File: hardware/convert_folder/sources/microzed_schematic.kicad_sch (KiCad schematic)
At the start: 5 parts, among them J4 87832-1420

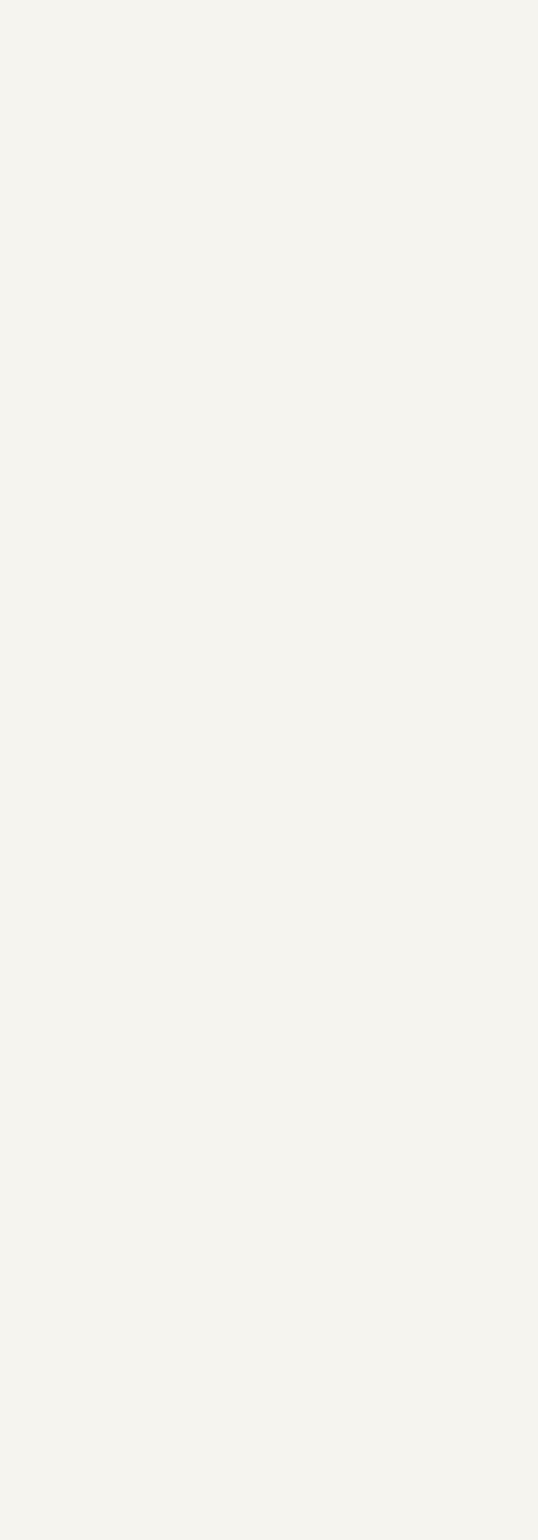
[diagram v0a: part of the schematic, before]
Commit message: fix: fix a lot of connections between blocks. Many more to go...
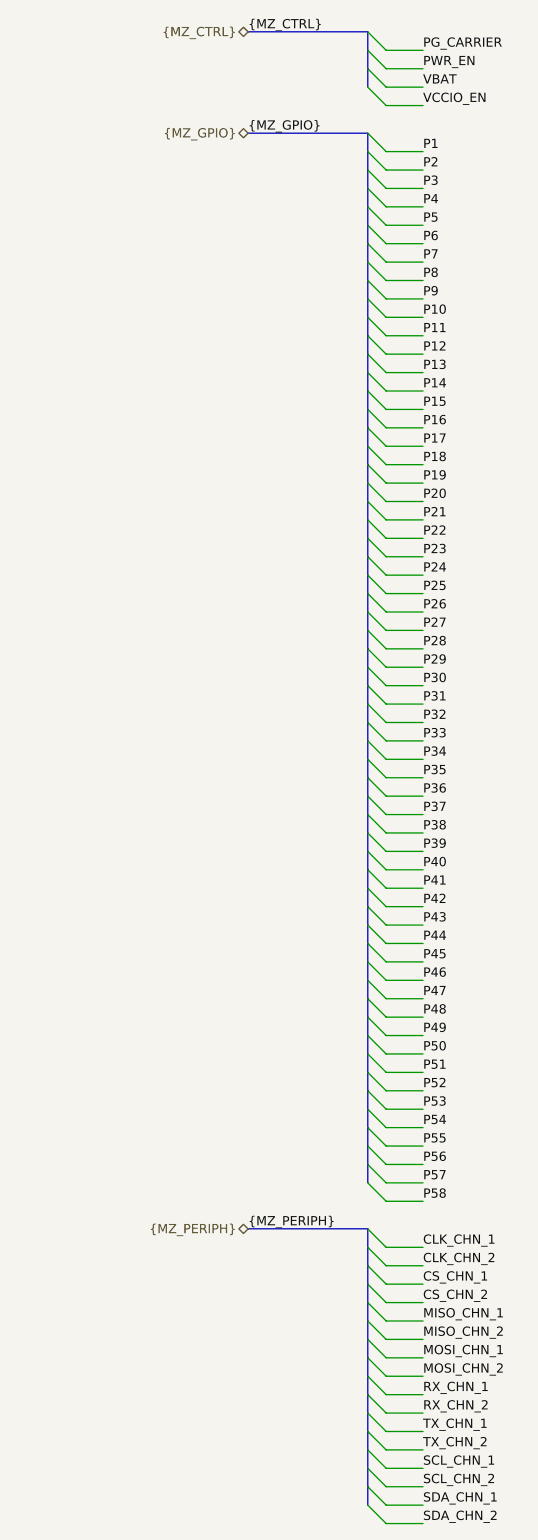
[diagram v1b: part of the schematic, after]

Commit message: fix: convert 90% of the schematic (there are 21 warnings/errors to resolve)
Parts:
- J4: footprint SAMTEC_TSW-107-05-F-D -> altium_import:SAMTEC_TSW-107-05-F-D; symbol flatsat_platform_2:root_0_87832-1420_flatsat_platform_2.SchLib -> altium_import:root_0_87832-1420_flatsat_platform_2.SchLib
- R13, R7, R8: footprint R0603_HD -> altium_import:R0603_HD; symbol Resistor:root_1_CRCW060350R0FKEA_Resistor.SchLib -> altium_import:root_1_CRCW060350R0FKEA_Resistor.SchLib
- SOM1: footprint MicroZedSOM -> altium_import:MICROZEDSOM; symbol flatsat_platform_2:root_0_MicroZed_SOM_flatsat_platform_2.SchLib -> altium_import:root_0_MicroZed_SOM_flatsat_platform_2.SchLib

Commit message: fix: start fixing the power converters of the board
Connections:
- net VBAT: no longer SOM1.JX1-7 (FPGA_VBATT)
- no-connect marks 22 -> 23

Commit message: fix: add more fixes to the power converters, add resets and other minor corrections
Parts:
- added C11, C9: 0.1uF/25V, altium_import:CC0805, symbol altium_import:root_1_Cap_Cer_X7R_0.1uF_25V_0805_flatsat_platform_2.SchLib
- added R37, R38: DNP, altium_import:0805, symbol altium_import:RDNP_0805
- added S10, S7: 430182043816, lib:430182043816, symbol lib:430182043816
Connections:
- net GND: now also C11.2, C9.2, S10.2 (NO_1), S10.4 (NO_2), S7.2 (NO_1), S7.4 (NO_2)
- net PG_CARRIER: now also S10.3 (COM_2)
- net CARRIER_SRST#: now reaches SOM1.JX1-6 (CARRIER_SRST#)
- net CARRIER_SRST#: now also S7.3 (COM_2)
- removed net VCCIO: SOM1.JX1-78 (VCCO_34), SOM1.JX1-79 (VCCO_34), SOM1.JX1-80 (VCCO_34), SOM1.JX2-78 (VCCO_35), SOM1.JX2-79 (VCCO_35), SOM1.JX2-80 (VCCO_35), SOM1.JX2-98 (VCCO_13)
- new net: C9.1, R37.1, S7.1 (COM_1)
- new net: C11.1, R38.1, S10.1 (COM_1)
- new net VCCIO_{13}: R37.2, R38.2, SOM1.JX2-98 (VCCO_13)
- new net VCCIO_{34}: SOM1.JX1-78 (VCCO_34), SOM1.JX1-79 (VCCO_34), SOM1.JX1-80 (VCCO_34)
- new net VCCIO_{35}: SOM1.JX2-78 (VCCO_35), SOM1.JX2-79 (VCCO_35), SOM1.JX2-80 (VCCO_35)
- no-connect marks 23 -> 22
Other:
- moved on the sheet: J4

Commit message: chore: add minor modifications do the layout
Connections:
- net VCCIO_{13}: no longer R37.2, R38.2
- new net VS: R37.2, R38.2
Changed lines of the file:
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@@
-		)
-	)
-	(label "VCCIO_{13}"
-		(at 83.82 39.37 180)
-		(effects
-			(font
-				(size 1.27 1.27)
-			)
-			(justify right bottom)
 		)
 	)
@@
 	(label "T/R_CHN_3"
 		(at 233.68 170.18 180)
-		(effects
-			(font
-				(size 1.27 1.27)
-			)
-			(justify right bottom)
-		)
-	)
-	(label "VCCIO_{13}"
-		(at 267.97 40.64 180)
 		(effects
 			(font
@@
 			)
 			(justify right)
+		)
+	)
+	(hierarchical_label "VS"
+		(shape input)
+		(at 83.82 39.37 180)
+		(effects
+			(font
+				(size 1.27 1.27)
+				(thickness 0.254)
+				(bold yes)
+			)
+			(justify right)
+		)
+	)
+	(hierarchical_label "VS"
+		(shape input)
+		(at 267.97 40.64 180)
+		(effects
+			(font
+				(size 1.27 1.27)
+				(thickness 0.254)
+				(bold yes)
+			)
+			(justify right)

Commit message: fix: fix the position of communication protocol signals on the MicroZed
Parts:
- removed R13, R7, R8: CRCW060350R0FKEA, altium_import:R0603_HD, symbol altium_import:root_1_CRCW060350R0FKEA_Resistor.SchLib
- added J19: 87832-1420, altium_import:SAMTEC_TSW-107-05-F-D, symbol altium_import:root_0_87832-1420_flatsat_platform_2.SchLib
- added R160, R39, R45, R46: CRCW060350R0FKEA, altium_import:R0603_HD, symbol altium_import:root_1_CRCW060350R0FKEA_Resistor.SchLib
- added R40, R47: DNP, altium_import:0805, symbol altium_import:RDNP_0805
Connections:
- net CLK_CHN_3: now also R39.1
- net CS_CHN_3: now also R46.2
- net GND: now also J19.14
- net MISO_CHN_3: now also R160.1; no longer SOM1.JX2-56 (JX2_LVDS_13_N)
- net MOSI_CHN_3: now also R45.2
- net RXD_CHN_2: now also SOM1.JX2-1 (MIO13); no longer SOM1.JX2-93 (BANK13_LVDS_4_P)
- net RX_CHN_3: now also SOM1.JX1-92 (BANK13_LVDS_3_P); no longer SOM1.JX2-62 (JX2_LVDS_15_P)
- net SCL_CHN_2: no longer SOM1.JX2-4 (MIO12)
- net SCL_CHN_3: now also SOM1.JX2-7 (MIO14), R47.1; no longer SOM1.JX2-49 (JX2_LVDS_10_N)
- net SDA_CHN_1: now also SOM1.JX2-50 (JX2_LVDS_11_N); no longer SOM1.JX2-63 (JX2_LVDS_14_N), SOM1.JX2-8 (MIO15)
- net SDA_CHN_2: no longer SOM1.JX2-1 (MIO13)
- net SDA_CHN_3: now also SOM1.JX2-8 (MIO15), R40.1; no longer SOM1.JX2-50 (JX2_LVDS_11_N)
- net T/R_CHN_3: now also SOM1.JX1-94 (BANK13_LVDS_3_N); no longer SOM1.JX2-64 (JX2_LVDS_15_N)
- net TXD_CHN_2: now also SOM1.JX2-4 (MIO12); no longer SOM1.JX2-95 (BANK13_LVDS_4_N)
- net TX_CHN_3: now also SOM1.JX1-89 (BANK13_LVDS_0_N); no longer SOM1.JX2-61 (JX2_LVDS_14_P)
- net VS: now also R40.2, R47.2
- net PL_JX2_12P: now reaches SOM1.JX2-53 (JX2_LVDS_12_P)
- net PL_JX2_12P: now also J19.2
- net PL_JX2_13P: now reaches SOM1.JX2-54 (JX2_LVDS_13_P)
- net PL_JX2_13P: now also J19.5
- net PL_JX2_12N: now reaches SOM1.JX2-55 (JX2_LVDS_12_N)
- net PL_JX2_12N: now also J19.4
- net at SOM1.JX2-68 (JX2_LVDS_17_P): now also J19.10; no longer SOM1.JX2-7 (MIO14)
- net at SOM1.JX2-94 (BANK13_LVDS_5_P): now also R39.2
- net at SOM1.JX2-96 (BANK13_LVDS_5_N): now also R160.2
- net PL_B13_6N: now reaches SOM1.JX2-99 (BANK13_LVDS_6_N)
- net PL_B13_6N: now also J19.13
- net PL_B13_2P: now reaches SOM1.JX1-91 (BANK13_LVDS_2_P)
- net PL_B13_2P: now also J19.1
- net PL_B13_2N: now reaches SOM1.JX1-93 (BANK13_LVDS_2_N)
- net PL_B13_2N: now also J19.3
- net P63 renamed PL_JX2_16N
- net P64 renamed PL_JX2_19P
- net P65 renamed PL_JX2_18P
- net P66 renamed PL_JX2_19N
- net P67 renamed PL_JX2_18N
- net P68 renamed PL_JX2_21P
- net P69 renamed PL_JX2_20P
- net P70 renamed PL_JX2_21N
- net P71 renamed PL_JX2_20N
- net P72 renamed PL_JX2_23P
- net P73 renamed PL_JX2_22P
- net P74 renamed PL_JX2_23N
- net P75 renamed PL_JX2_22N
- new net: R45.1, SOM1.JX2-93 (BANK13_LVDS_4_P)
- new net: R46.1, SOM1.JX2-95 (BANK13_LVDS_4_N)
- new net PL_JX2_13N: J19.7, SOM1.JX2-56 (JX2_LVDS_13_N)
- new net PL_JX2_14N: J19.8, SOM1.JX2-63 (JX2_LVDS_14_N)
- new net PL_JX2_14P: J19.6, SOM1.JX2-61 (JX2_LVDS_14_P)
- new net PL_JX2_15N: J19.11, SOM1.JX2-64 (JX2_LVDS_15_N)
- new net PL_JX2_15P: J19.9, SOM1.JX2-62 (JX2_LVDS_15_P)
- new net SCL_CHN_1: SOM1.JX2-49 (JX2_LVDS_10_N)
- no-connect marks 22 -> 15
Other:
- moved on the sheet: C11, C9, J4, R37, R38, S10, S7, SOM1A, SOM1B

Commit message: fix: fix position of components and signals routing
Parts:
- removed J19, J4: 87832-1420, altium_import:SAMTEC_TSW-107-05-F-D, symbol altium_import:root_0_87832-1420_flatsat_platform_2.SchLib
- added J20, J21: 61201421621, lib:61201421621, symbol lib:61201421621
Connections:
- net GND: now also J20.1, J21.1, J21.2
- net PL_B13_2N: now also J21.11
- net PL_B13_2P: now also J21.13
- net PL_B13_6N: now also J21.14
- net PL_JX2_12N: now also J21.7
- net PL_JX2_12P: now also J21.9
- net PL_JX2_13N: now also J21.6
- net PL_JX2_13P: now also J21.4
- net PL_JX2_14N: now also J21.3
- net PL_JX2_14P: now also J21.5
- net PL_JX2_15N: now also J21.10
- net PL_JX2_15P: now also J21.8
- net PL_JX2_16N: now also J20.2
- net PL_JX2_18N: now also J20.6
- net PL_JX2_18P: now also J20.4
- net PL_JX2_19N: now also J20.5
- net PL_JX2_19P: now also J20.3
- net PL_JX2_20N: now also J20.10
- net PL_JX2_20P: now also J20.8
- net PL_JX2_21N: now also J20.9
- net PL_JX2_21P: now also J20.7
- net PL_JX2_22N: now also J20.14
- net PL_JX2_22P: now also J20.12
- net PL_JX2_23N: now also J20.13
- net PL_JX2_23P: now also J20.11
- net at SOM1.JX2-68 (JX2_LVDS_17_P): now also J21.12
- no-connect marks 15 -> 14
